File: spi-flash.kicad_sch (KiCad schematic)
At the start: 14 parts, among them J4 Tag-Connect_TC2050-IDC-NL_2x5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, U14 MT25QL01GBBB8E_SOP2-16

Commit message: [#95398] Add markings for ETH strap resistors
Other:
- title: renode-reference-platform -> STM32H7 Renode Reference Platform
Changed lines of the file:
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@@
 	(paper "A3")
 	(title_block
-		(title "renode-reference-platform")
+		(title "STM32H7 Renode Reference Platform")
 		(date "07.04.2026")
 		(rev "1.0.0")

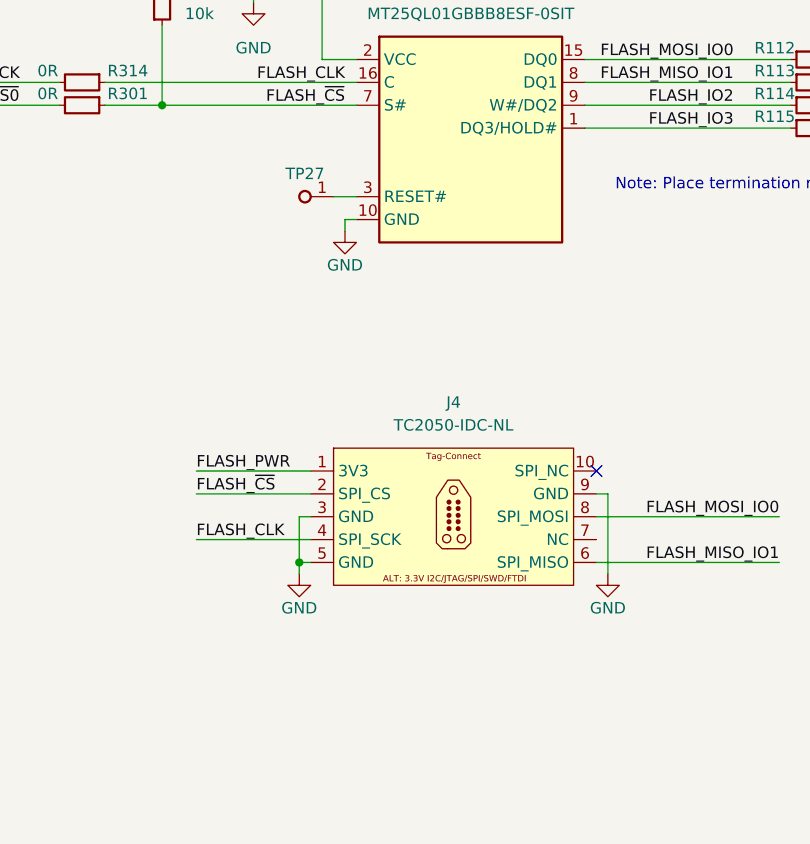
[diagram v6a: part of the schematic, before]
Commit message: [#95451] Fiducial and TP placement
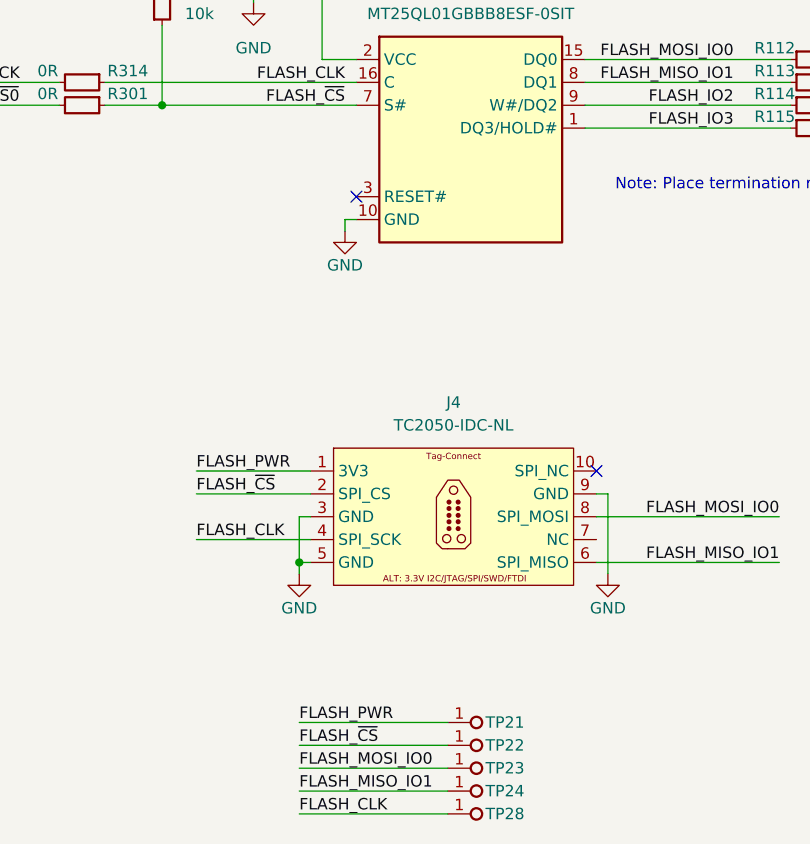
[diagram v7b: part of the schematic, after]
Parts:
- removed TP27: TP_1mm_SMD, antmicro-footprints:TP_SMD_1mm, symbol antmicroTestPoints:TP_1mm_SMD
- added TP21, TP22, TP23, TP24, TP28: TP_0.75mm_SMD, antmicro-footprints:TP_SMD_1mm, symbol antmicroTestPoints:TP_1mm_SMD
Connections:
- net FLASH_CLK: now also TP28.1
- net FLASH_MISO_IO1: now also TP24.1
- net FLASH_MOSI_IO0: now also TP23.1
- net FLASH_PWR: now also TP21.1
- net FLASH_~{CS}: now also TP22.1
- no-connect marks 1 -> 2

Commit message: [#96159] Start PCB layout
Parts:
- added TP30: TP_0.75mm_SMD, antmicro-footprints:TP_SMD_1mm, symbol antmicroTestPoints:TP_1mm_SMD
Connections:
- net FLASH_~{CS}: no longer R345.1
- net GND: now also TP30.1
- net SPI_Flash.~{CS0}: now also R345.1
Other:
- moved on the sheet: R301, R314, R345
